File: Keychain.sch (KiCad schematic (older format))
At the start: 0 parts

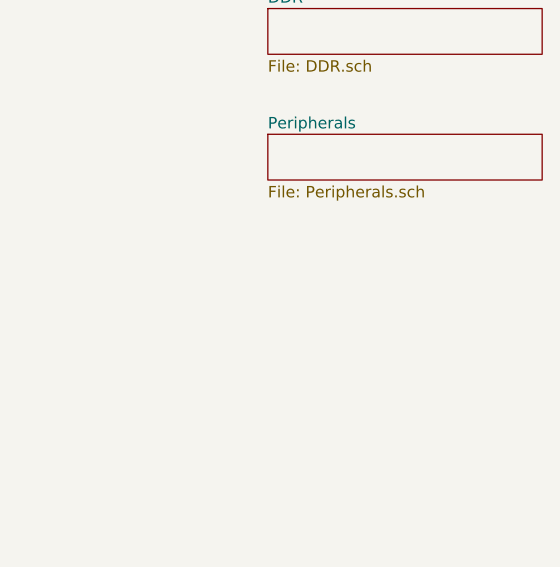
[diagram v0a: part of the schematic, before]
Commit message: Added some LDO and connectors, still need to finish routing
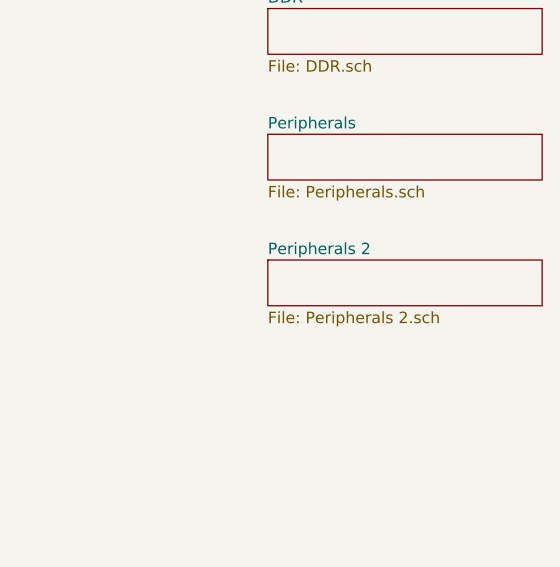
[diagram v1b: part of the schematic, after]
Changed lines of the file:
@@
 $Descr A4 11693 8268
 encoding utf-8
-Sheet 1 4
+Sheet 1 5
 Title ""
 Date ""
@@
 F1 "DDR.sch" 50
 $EndSheet
+$Sheet
+S 4700 2800 1200 200
+U 5FC11E82
+F0 "Peripherals 2" 50
+F1 "Peripherals 2.sch" 50
+$EndSheet
 $EndSCHEMATC

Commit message: New layout!
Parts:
- added C1, C16, C18, C22, C7: 22uF, Capacitor_SMD:C_0603_1608Metric, symbol Device:C
- added C10, C11, C12, C13, C15, C17, C3, C5, C8, C9: 0.22uF, Capacitor_SMD:C_0402_1005Metric, symbol Device:C
- added C14, C19, C20, C6: 10uF, Capacitor_SMD:C_0603_1608Metric, symbol Device:C
- added C2, C4: 4.7uF, Capacitor_SMD:C_0402_1005Metric, symbol Device:C
- added C21: 22uF, Capacitor_SMD:C_0603_1608Metric, symbol Device:CP1
- added C23, C25, C27, C36, C37, C38, C39: 0.22uF, Capacitor_SMD:C_0402_1005Metric, symbol Device:CP1
- added C30, C32: 18pF, Capacitor_SMD:C_0402_1005Metric, symbol Device:C
- added C44, C45: 0.1uF, Capacitor_SMD:C_0402_1005Metric, symbol Device:CP1
- added C46, C47: 2.2pF, Capacitor_SMD:C_0402_1005Metric, symbol Device:CP1
- added J1: Micro_SD_Card, Connector_Card:microSD_HC_Molex_104031-0811, symbol Connector:Micro_SD_Card
- added J2: Conn_01x04, Connector_PinHeader_2.54mm:PinHeader_1x05_P2.54mm_Vertical, symbol Connector_Generic:Conn_01x05
- added J3: USB_A, Connector_USB:USB_A_Molex_67643_Horizontal, symbol Connector:USB_A
- added R1, R3: 10K, Resistor_SMD:R_0402_1005Metric, symbol Device:R
- added R4, R8: 240, Resistor_SMD:R_0402_1005Metric, symbol Device:R
- added R5: 470, Resistor_SMD:R_0402_1005Metric, symbol Device:R
- added R6, R7: 1.5K, Resistor_SMD:R_0402_1005Metric, symbol Device:R
- added U1: IMX6UL_BGA289, Custom Components:IMX6UL_BGA289, symbol custom_components:IMX6UL_BGA289
- added U2: DDR3_BGA96, Custom Components:DDR3_BGA96, symbol custom_components:DDR3_BGA96
- added U3: AZ1117C-3.3, Package_TO_SOT_SMD:SOT-223, symbol Regulator_Linear:AZ1117-3.3
- added U4: AZ1117C-1.5, Package_TO_SOT_SMD:SOT-223, symbol Regulator_Linear:AZ1117-1.5
- added Y1: Crystal_GND24, Crystal:Crystal_SMD_3225-4Pin_3.2x2.5mm, symbol Device:Crystal_GND24
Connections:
- net labels added: +1V5, +3.3V, +5V, A0, A1, A10, A11, A12, A13, A14, A2, A3, A4, A5, A6, A7, A8, A9, ARM_CAP, BA0, BA1, BA2, CAS#, CK+, CK-, CKE0, CS0#, CTS, DML, DMU, DQL0, DQL1, DQL2, DQL3, DQL4, DQL5, DQL6, DQL7, DQSL+, DQSL-, DQSU+, DQSU-, DQU0, DQU1, DQU2, DQU3, DQU4, DQU5, DQU6, DQU7, GND, HIGH_CAP, NVCC_PLL, ODT0, RAS#, RESET#, RTS, RX, SD_CLK, SD_CMD, SD_D0, SD_D1, SD_D2, SD_D3, SNVS_CAP, SOC_CAP, TX, VDD_HIGH_CAP, VREFDDR, WE#, XTALI, XTALO, ZQ, ZQPAD
- wire segments 0 -> 510
- no-connect marks 0 -> 141
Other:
- note added: "CLK Termination\nClose to DDR3 chip"
- note added: "CLK Termination\nPlace C close to\nDDR3 chip"
- note added: "Close to DDR3"
- note added: "Close to \nDDR3 VREFCA"
- note added: "Close to \nDDR3 VREFDQ"
- note added: "Data lines in bold\nare intentionally\nswapped to simplify \nrouting."

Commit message: New layout
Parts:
- U3: value AZ1117C-3.3 -> AZ1117H-3.3; LCSC C108492 -> C92517
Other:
- moved on the sheet: U1F
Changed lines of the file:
@@
 AR Path="/6250E312" Ref="U3"  Part="1"
 F 0 "U3" H 3000 1342 50  0000 C CNN
-F 1 "AZ1117C-3.3" H 3000 1251 50  0000 C CNN
+F 1 "AZ1117H-3.3" H 3000 1251 50  0000 C CNN
 F 2 "Package_TO_SOT_SMD:SOT-223" H 3000 1350 50  0001 C CIN
 F 3 "https://datasheet.lcsc.com/szlcsc/Diodes-Incorporated-AZ1117EH-3-3TRG1_C108494.pdf" H 3000 1100 50  0001 C CNN
-F 4 "C108492" H 3000 1100 50  0001 C CNN "LCSC"
+F 4 "C92517" H 3000 1100 50  0001 C CNN "LCSC"
 	1    3000 1100
 	1    0    0    -1
@@
 RTS
 Wire Wire Line
-	3000 1500 3000 1550
-Wire Wire Line
 	8450 4100 8950 4100
 $Comp
@@
 	1    0    0    -1
 $EndComp
-NoConn ~ 15850 4600
-NoConn ~ 15850 4700
-NoConn ~ 15850 4800
-NoConn ~ 15850 4900
-NoConn ~ 15850 5000
-NoConn ~ 15850 5100
-NoConn ~ 15850 5200
-NoConn ~ 15850 5300
-NoConn ~ 15850 5400
-NoConn ~ 15850 5500
-NoConn ~ 15850 5600
-NoConn ~ 15850 5700
-NoConn ~ 15850 5800
-NoConn ~ 15850 5900
-NoConn ~ 15850 6000
-NoConn ~ 15850 6100
-NoConn ~ 15900 9600
-NoConn ~ 15900 9500
-NoConn ~ 15900 9400
-NoConn ~ 15900 9300
-NoConn ~ 15900 9200
-NoConn ~ 15900 9100
-NoConn ~ 15900 9000
-NoConn ~ 15900 8900
-NoConn ~ 15900 8800
-NoConn ~ 15900 8700
+NoConn ~ 15950 4600
+NoConn ~ 15950 4700
+NoConn ~ 15950 4800
+NoConn ~ 15950 4900
+NoConn ~ 15950 5000
+NoConn ~ 15950 5100
+NoConn ~ 15950 5200
+NoConn ~ 15950 5300
+NoConn ~ 15950 5400
+NoConn ~ 15950 5500
+NoConn ~ 15950 5600
+NoConn ~ 15950 5700
+NoConn ~ 15950 5800
+NoConn ~ 15950 5900
+NoConn ~ 15950 6000
+NoConn ~ 15950 6100
+NoConn ~ 15950 9600
+NoConn ~ 15950 9500
+NoConn ~ 15950 9400
+NoConn ~ 15950 9300
+NoConn ~ 15950 9200
+NoConn ~ 15950 9100
+NoConn ~ 15950 9000
+NoConn ~ 15950 8900
+NoConn ~ 15950 8800
+NoConn ~ 15950 8700
 $Comp
 L custom_components:IMX6UL_BGA289 U?
@@
 L custom_components:IMX6UL_BGA289 U?
 U 6 1 6250E44D
-P 15100 4400
+P 15100 4350
 AR Path="/5FD79E88/6250E44D" Ref="U?"  Part="6"
 AR Path="/5FC11E82/6250E44D" Ref="U?"  Part="6"
 AR Path="/5FAE186D/6250E44D" Ref="U?"  Part="6"
 AR Path="/6250E44D" Ref="U1"  Part="6"
-F 0 "U1" H 15100 4587 60  0000 C CNN
-F 1 "IMX6UL_BGA289" H 15100 4481 60  0000 C CNN
-F 2 "Custom Components:IMX6UL_BGA289" H 16700 2500 60  0001 C CNN
-F 3 "" H 16700 2500 60  0001 C CNN
-F 4 "C394784" H 15100 4400 50  0001 C CNN "LCSC"
-	6    15100 4400
+F 0 "U1" H 15100 4537 60  0000 C CNN
+F 1 "IMX6UL_BGA289" H 15100 4431 60  0000 C CNN
+F 2 "Custom Components:IMX6UL_BGA289" H 16700 2450 60  0001 C CNN
+F 3 "" H 16700 2450 60  0001 C CNN
+F 4 "C394784" H 15100 4350 50  0001 C CNN "LCSC"
+	6    15100 4350
 	1    0    0    -1
 $EndComp
@@
 L power:+3.3V #PWR?
 U 1 1 6250E453
-P 14200 4600
+P 14200 4550
 AR Path="/5FD79E88/6250E453" Ref="#PWR?"  Part="1"
 AR Path="/5FC11E82/6250E453" Ref="#PWR?"  Part="1"
 AR Path="/5FAE186D/6250E453" Ref="#PWR?"  Part="1"
 AR Path="/6250E453" Ref="#PWR0133"  Part="1"
-F 0 "#PWR0133" H 14200 4450 50  0001 C CNN
-F 1 "+3.3V" H 14215 4773 50  0000 C CNN
-F 2 "" H 14200 4600 50  0001 C CNN
-F 3 "" H 14200 4600 50  0001 C CNN
-	1    14200 4600
-	1    0    0    -1
-$EndComp
-Wire Wire Line
-	14200 4650 14200 4600
-NoConn ~ 14250 6150
-NoConn ~ 14250 6050
-NoConn ~ 14250 5950
-NoConn ~ 14250 5850
-NoConn ~ 14250 5750
-NoConn ~ 14250 5650
-NoConn ~ 14250 5550
-NoConn ~ 14250 5450
-NoConn ~ 14250 5250
-NoConn ~ 14250 5150
-NoConn ~ 14250 5050
-NoConn ~ 14250 4950
-NoConn ~ 14250 4850
-Wire Wire Line
-	14200 4650 14250 4650
+F 0 "#PWR0133" H 14200 4400 50  0001 C CNN
+F 1 "+3.3V" H 14215 4723 50  0000 C CNN
+F 2 "" H 14200 4550 50  0001 C CNN
+F 3 "" H 14200 4550 50  0001 C CNN
+	1    14200 4550
+	1    0    0    -1
+$EndComp
+Wire Wire Line
+	14200 4600 14200 4550
+NoConn ~ 14250 6100
+NoConn ~ 14250 6000
+NoConn ~ 14250 5900
+NoConn ~ 14250 5800
+NoConn ~ 14250 5700
+NoConn ~ 14250 5600
+NoConn ~ 14250 5500
+NoConn ~ 14250 5400
+NoConn ~ 14250 5200
+NoConn ~ 14250 5100
+NoConn ~ 14250 5000
+NoConn ~ 14250 4900
+NoConn ~ 14250 4800
+Wire Wire Line
+	14200 4600 14250 4600
 $Comp
 L custom_components:IMX6UL_BGA289 U?
@@
 Wire Wire Line
 	5550 1150 5550 2150
+Wire Wire Line
+	3000 1400 3000 1550
 Wire Bus Line
 	1450 9250 8650 9250
